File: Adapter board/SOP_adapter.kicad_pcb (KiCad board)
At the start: 2 copper layers, 110 x 100 mm, 23 parts, among them J1 Conn_01x03_Female, J2 Conn_01x24_Female, J3 Conn_01x24_Female, U1 AMS1117-3.3, U2 STM32F103C8Tx

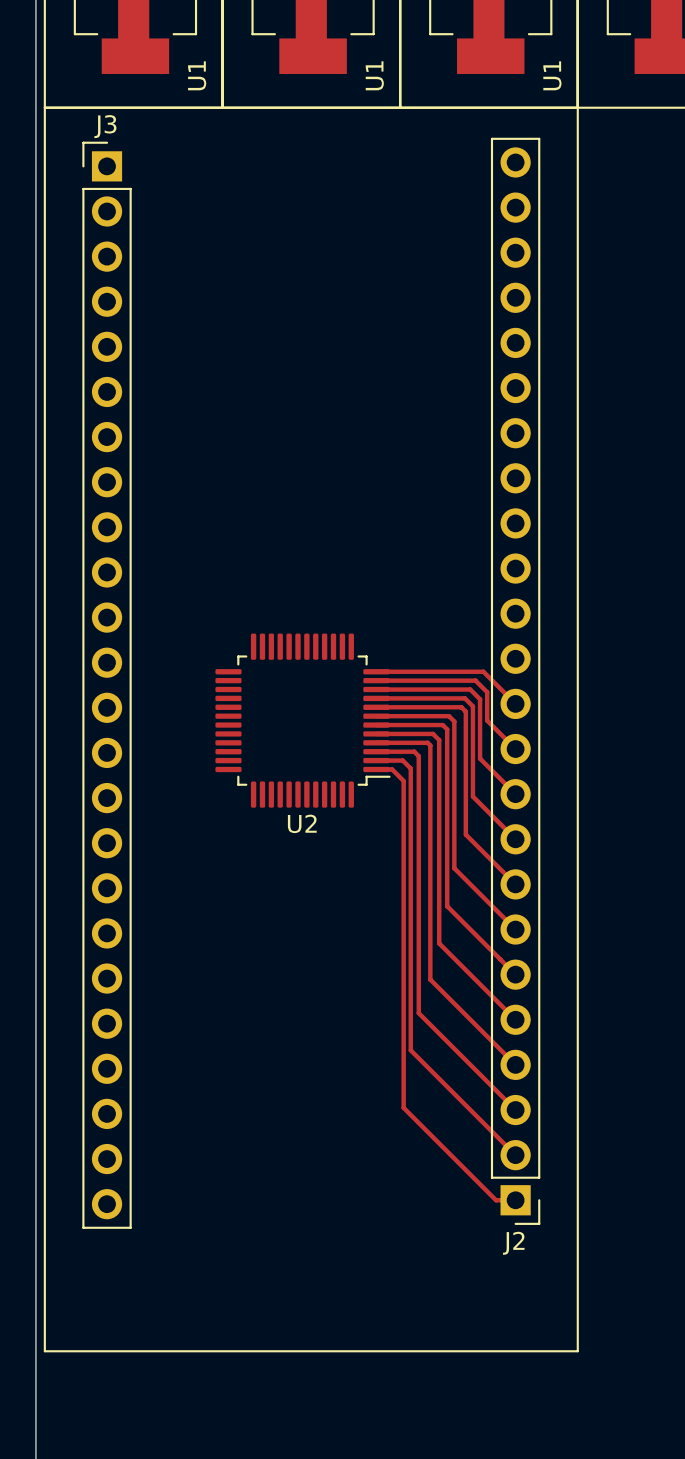
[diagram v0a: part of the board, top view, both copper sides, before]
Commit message: Add files via upload
updated qfnp48 header pins to 02x06
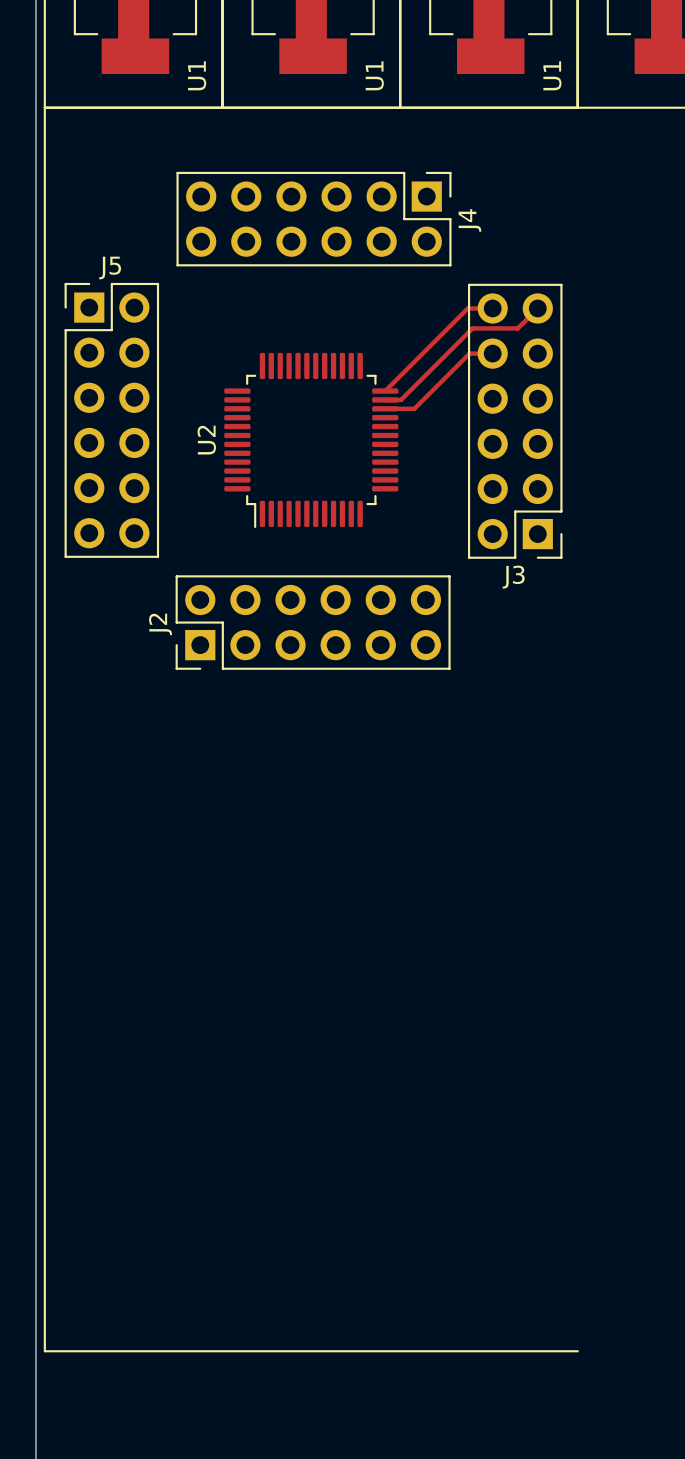
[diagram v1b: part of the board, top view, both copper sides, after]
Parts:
- added J4: Conn_02x06_Counter_Clockwise, Connector_PinHeader_2.54mm:PinHeader_2x06_P2.54mm_Vertical, F.Cu at (-138.0, 20.5)
- added J5: Conn_02x06_Counter_Clockwise, Connector_PinHeader_2.54mm:PinHeader_2x06_P2.54mm_Vertical, F.Cu at (-157.0, 26.8)
- J2, J3: value Conn_01x24_Female -> Conn_02x06_Counter_Clockwise; footprint Connector_PinHeader_2.54mm:PinHeader_1x24_P2.54mm_Vertical -> Connector_PinHeader_2.54mm:PinHeader_2x06_P2.54mm_Vertical
- moved J2 35.9 mm to (-150.8, 45.8), turned to 90 degrees
- moved J3 31.9 mm to (-131.8, 39.5), turned to 180 degrees
- moved U2 15.8 mm to (-144.5, 34.2), turned to 90 degrees
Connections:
- net Net-(J2-Pad5) renamed 5
- net Net-(J2-Pad6) renamed 6
- J3 pad 1: 25 -> 13
- J3 pad 10: 34 -> 22
- J3 pad 11: 35 -> 23
- J3 pad 12: 36 -> 24
- J3 pad 2: 26 -> 14
- J3 pad 3: 27 -> 15
- J3 pad 4: 28 -> 16
- J3 pad 5: 29 -> 17
- J3 pad 6: 30 -> 18
- J3 pad 7: 31 -> 19
- J3 pad 8: 32 -> 20
- J3 pad 9: 33 -> 21
- U2 pad 18: Net-(J2-Pad18) -> 18
- U2 pad 19: Net-(J2-Pad19) -> 19
- U2 pad 20: Net-(J2-Pad20) -> 20
- U2 pad 21: Net-(J2-Pad21) -> 21
- U2 pad 22: Net-(J2-Pad22) -> 22
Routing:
- net 1: track 28.7 -> 0.00 mm
- net 2: track 26.3 -> 0.00 mm
- net 3: track 24.7 -> 0.00 mm
- net 4: track 23.1 -> 0.00 mm
- net 5: track 21.2 -> 0.00 mm
- net 6: track 19.5 -> 0.00 mm
- net 7: track 17.7 -> 0.00 mm
- net 8: track 16.0 -> 0.00 mm
- net 9: track 14.1 -> 0.00 mm
- net 10: track 12.2 -> 0.00 mm
- net 23: track 0.00 -> 10.7 mm
- net 11: track 10.4 -> 0.00 mm
- net 12: track 8.59 -> 0.00 mm
- net 24: track 0.00 -> 7.97 mm
- net 22: track 0.00 -> 7.34 mm
